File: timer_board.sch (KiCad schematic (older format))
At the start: 40 parts

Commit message: Added Reset
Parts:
- added R?: 10k, ~, symbol R
- added S?: RESET, ~, symbol RESET
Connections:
- wire segments 134 -> 139
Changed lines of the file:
@@
-EESchema Schematic File Version 2  date 7/2/2013 10:27:25 PM
+EESchema Schematic File Version 2  date 7/2/2013 10:32:23 PM
 LIBS:power
 LIBS:device
@@
 Wire Wire Line
 	10325 3000 10325 3150
-Text GLabel 6175 2200 0    47   Input ~ 0
+Text GLabel 6200 2350 0    47   Input ~ 0
 reset
-Wire Wire Line
-	6175 2200 6700 2200
 Text GLabel 9450 3025 0    47   Input ~ 0
 reset
@@
 Wire Wire Line
 	6500 4100 6500 3900
+$Comp
+L R R?
+U 1 1 51D3AA45
+P 5900 1950
+F 0 "R?" V 5825 1950 40  0000 C CNN
+F 1 "10k" V 5907 1951 40  0000 C CNN
+F 2 "~" V 5830 1950 30  0000 C CNN
+F 3 "~" H 5900 1950 30  0000 C CNN
+	1    5900 1950
+	1    0    0    -1
+$EndComp
+$Comp
+L RESET S?
+U 1 1 51D3AA4B
+P 5400 2100
+F 0 "S?" H 5300 2350 50  0000 L BNN
+F 1 "RESET" H 5300 1850 50  0000 L BNN
+F 2 "~" H 5400 2250 50  0001 C CNN
+F 3 "~" H 5400 2100 60  0000 C CNN
+	1    5400 2100
+	1    0    0    -1
+$EndComp
+Wire Wire Line
+	5600 2200 6700 2200
+$Comp
+L +5V #PWR?
+U 1 1 51D3ABC0
+P 5900 1600
+F 0 "#PWR?" H 5900 1690 20  0001 C CNN
+F 1 "+5V" H 5900 1690 30  0000 C CNN
+F 2 "" H 5900 1600 60  0000 C CNN
+F 3 "" H 5900 1600 60  0000 C CNN
+	1    5900 1600
+	1    0    0    -1
+$EndComp
+Wire Wire Line
+	5900 1600 5900 1700
+Connection ~ 5900 2200
+Wire Wire Line
+	5200 2100 5200 2200
+$Comp
+L GND #PWR?
+U 1 1 51D3AE8D
+P 5050 2300
+F 0 "#PWR?" H 5050 2300 30  0001 C CNN
+F 1 "GND" H 5050 2230 30  0001 C CNN
+F 2 "" H 5050 2300 60  0000 C CNN
+F 3 "" H 5050 2300 60  0000 C CNN
+	1    5050 2300
+	1    0    0    -1
+$EndComp
+Wire Wire Line
+	5050 2300 5050 2200
+Wire Wire Line
+	5050 2200 5200 2200
+Wire Wire Line
+	6200 2350 6200 2200
+Connection ~ 6200 2200
 $EndSCHEMATC

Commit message: Grounded switches, added trigger and output
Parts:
- added C?: 1uF, ~, symbol C
- added C?: CP1, ~, symbol CP1
- added D?: Relay, ~, symbol LED
- added D?: Trigger, ~, symbol LED
- added P?: OUT_INV, symbol CONN_2
- added P? (x2): OUT, symbol CONN_2
- added R?: 1k, ~, symbol R
- added R? (x2): 2.2k, ~, symbol R
- added U? (x4): 74HC04, ~, symbol 74HC04
- D?: value LED -> Power
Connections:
- wire segments 139 -> 164
- no-connect marks 3 -> 12

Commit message: Fixed up a few bad connections
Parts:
- added RV1: POT, ~, symbol POT
- gave numbers to parts that had none: 53
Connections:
- wire segments 164 -> 170
- no-connect marks 12 -> 13

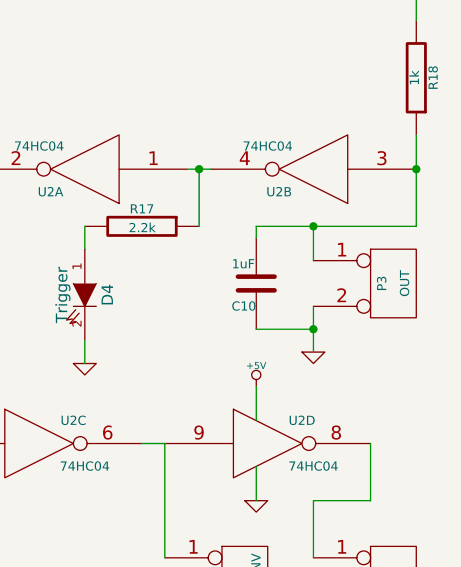
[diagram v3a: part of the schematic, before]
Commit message: Started workin on layout
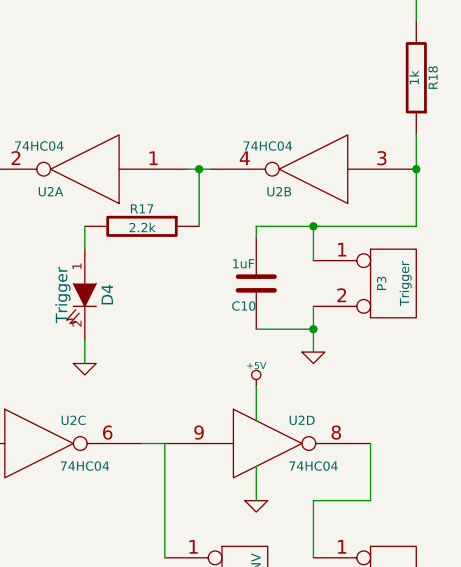
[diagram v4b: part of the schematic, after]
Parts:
- P3: value OUT -> Trigger
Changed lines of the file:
@@
-EESchema Schematic File Version 2  date 7/3/2013 11:54:40 PM
+EESchema Schematic File Version 2  date 7/4/2013 12:06:58 AM
 LIBS:power
 LIBS:device
@@
 P 11000 4650
 F 0 "P3" V 10950 4650 40  0000 C CNN
-F 1 "OUT" V 11050 4650 40  0000 C CNN
+F 1 "Trigger" V 11050 4650 40  0000 C CNN
 F 2 "" H 11000 4650 60  0000 C CNN
 F 3 "" H 11000 4650 60  0000 C CNN
